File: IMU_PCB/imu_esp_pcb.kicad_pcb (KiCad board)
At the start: 2 copper layers, 19 parts, among them J3 Conn_01x02_Pin, U1 MPU-6050, U2 ESP32-C3-WROOM-02, U3 PTS647SM38SMTR2LFS, U4 XC6206P332MR-G, U5 1N5819HW-7-F

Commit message: Add files via upload
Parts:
- added R4: 0, Resistor_SMD:R_0805_2012Metric_Pad1.20x1.40mm_HandSolder, F.Cu at (104.5, 87.0)
- added R5: 0, Resistor_SMD:R_0805_2012Metric_Pad1.20x1.40mm_HandSolder, F.Cu at (95.0, 90.5)
- added R6: 0, Resistor_SMD:R_0805_2012Metric_Pad1.20x1.40mm_HandSolder, F.Cu at (94.0, 71.0)
- moved C4 2.00 mm to (92.5, 84.5)
- moved C1 2.00 mm to (95.0, 84.5)
- moved C9 0.96 mm to (98.5, 80.5)
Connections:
- U1 pad 24: SDA -> Net-(U1-SDA)
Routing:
- net GND: track 2.65 -> 36.1 mm
- net SDA: track 14.8 -> 5.22 mm, vias 2 -> 0
- net Net-(U1-SDA): track 0.00 -> 6.98 mm
- net Net-(U4-VIN): track 11.6 -> 9.58 mm
- net Net-(U1-CPOUT): track 10.8 -> 9.54 mm
- net Net-(U1-REGOUT): track 8.42 -> 7.60 mm
- net Net-(U1-VLOGIC): track 8.65 -> 9.17 mm
- net +3.3V: track 90.9 -> 91.3 mm, vias 2 -> 0
- removed copper zone on B.Cu, net GND
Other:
- board outline added: 48.5 x 26 mm

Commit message: we're cooked
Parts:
- removed J3: Conn_01x02_Pin, Connector_PinHeader_2.54mm:PinHeader_1x02_P2.54mm_Vertical_SMD_Pin1Left
- removed UART1: UART, Connector_PinHeader_2.54mm:PinHeader_1x04_P2.54mm_Vertical
- added J1: Conn_01x02_Pin, Connector_PinHeader_2.54mm:PinHeader_1x02_P2.54mm_Vertical, F.Cu at (88.5, 87.0)
- added J2: Conn_01x05_Pin, Connector_PinHeader_2.54mm:PinHeader_1x05_P2.54mm_Vertical, F.Cu at (66.5, 75.9)
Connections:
- U1 pad 12: GND -> unconnected-(U1-INT-Pad12)
- U2 pad 11: unconnected-(U2-IO20/RXD-Pad11) -> TXD
- U2 pad 12: unconnected-(U2-IO21/TXD-Pad12) -> RXD
- U2 pad 6: Net-(U2-IO7) -> unconnected-(U2-IO7-Pad6)
- U2 pad 7: Net-(U2-IO8) -> unconnected-(U2-IO8-Pad7)
- U2 pad 8: unconnected-(U2-IO9-Pad8) -> Net-(J2-Pin_4)
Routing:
- net RXD: track 0.00 -> 27.8 mm
- net TXD: track 0.00 -> 27.0 mm
- net +3.3V: track 91.3 -> 117.7 mm
- net Net-(J2-Pin_4): track 0.00 -> 16.0 mm
- net GND: track 36.1 -> 45.7 mm, vias 0 -> 2
- net Net-(U2-IO8): track 8.33 -> 0.00 mm
- net Net-(U2-IO7): track 7.90 -> 0.00 mm
- net RESET: track 40.2 -> 43.1 mm
- net Net-(J1-Pin_1): track 4.96 -> 4.24 mm

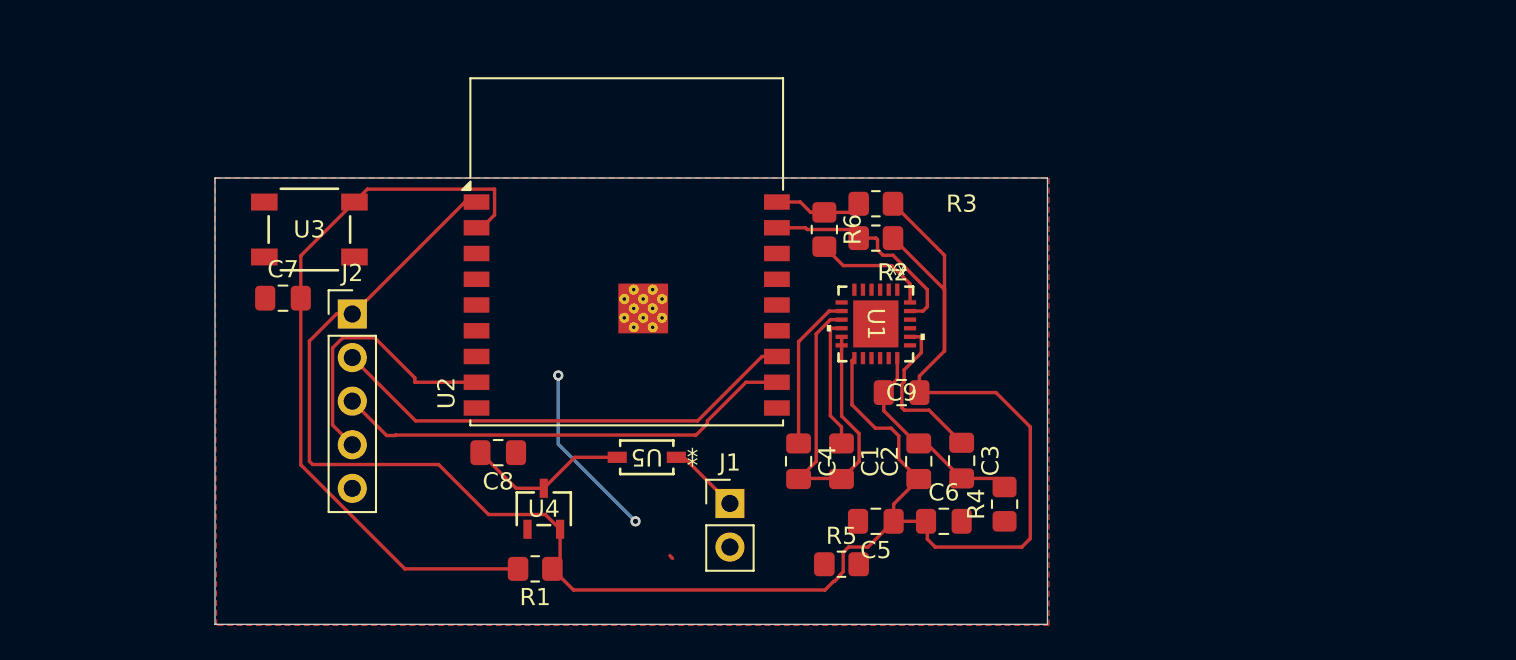
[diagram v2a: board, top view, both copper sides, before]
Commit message: Fixing PCB files from root
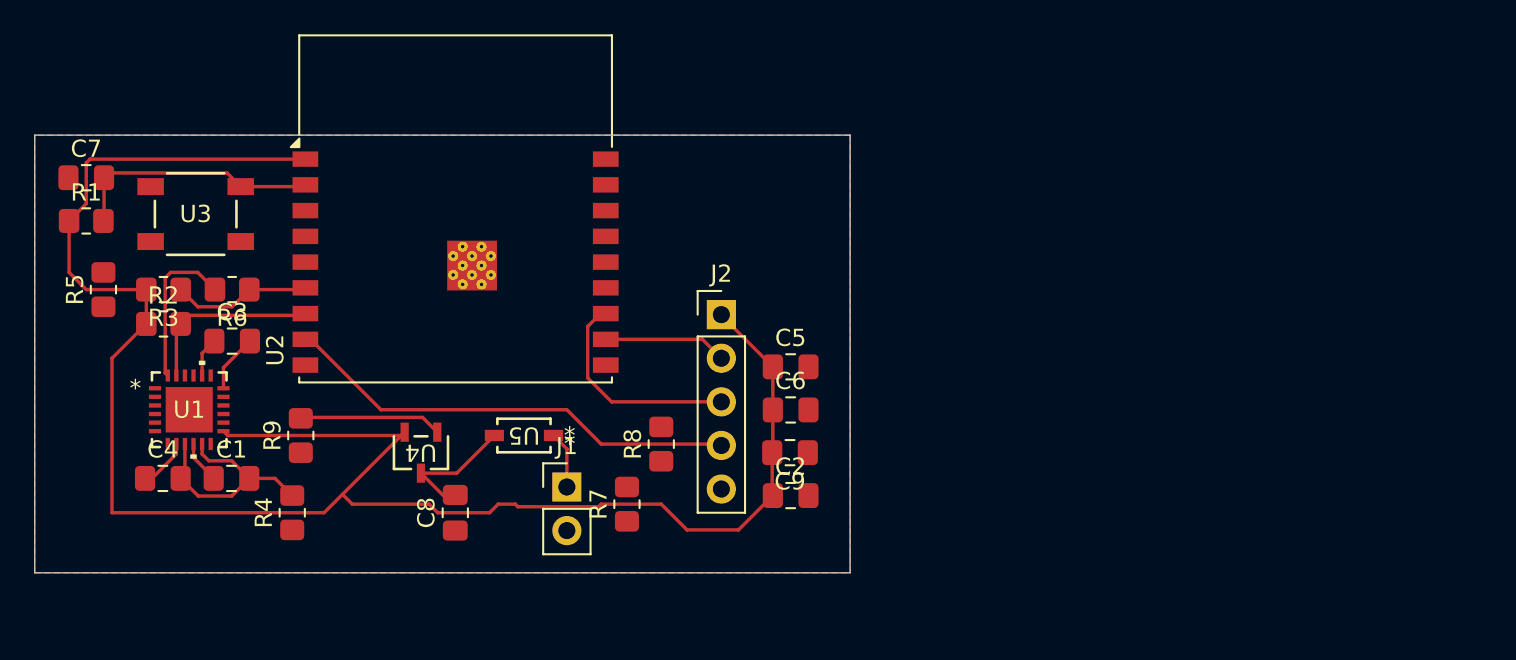
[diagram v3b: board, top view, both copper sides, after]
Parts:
- added R7: 0, Resistor_SMD:R_0805_2012Metric_Pad1.20x1.40mm_HandSolder, F.Cu at (82.5, 87.0)
- added R8: 0, Resistor_SMD:R_0805_2012Metric_Pad1.20x1.40mm_HandSolder, F.Cu at (84.5, 83.5)
- added R9: 0, Resistor_SMD:R_0805_2012Metric_Pad1.20x1.40mm_HandSolder, F.Cu at (63.5, 83.0)
- moved R5 45.9 mm to (52.0, 74.5), turned to 90 degrees
- moved C3 43.1 mm to (59.5, 77.5), turned to 0 degrees
- moved R2 41.8 mm to (55.5, 76.5), turned to 0 degrees
- moved R3 41.8 mm to (55.5, 74.5), turned to 180 degrees
- moved R4 41.5 mm to (63.0, 87.5)
- moved U1 40.3 mm to (57.0, 81.5), turned to 0 degrees
- moved C4 37.1 mm to (55.5, 85.5), turned to 0 degrees
- moved C1 35.6 mm to (59.5, 85.5), turned to 0 degrees
- moved R6 34.7 mm to (59.5, 74.5), turned to 180 degrees
- moved R1 33.1 mm to (51.0, 70.5), turned to 0 degrees
- moved J2 21.5 mm to (88.0, 76.0)
- moved C7 13.4 mm to (51.0, 68.0)
- moved C6 11.0 mm to (92.0, 81.5)
- moved U2 10.3 mm to (72.5, 72.9)
- moved C5 10.3 mm to (92.0, 79.0), turned to 0 degrees
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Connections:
- U2 pad 11: TXD -> RXD
- U2 pad 12: RXD -> TXD
- U2 pad 17: SCL -> unconnected-(U2-IO1-Pad17)
- U2 pad 18: SDA -> unconnected-(U2-IO0-Pad18)
- U2 pad 6: unconnected-(U2-IO7-Pad6) -> SDA
- U2 pad 7: unconnected-(U2-IO8-Pad7) -> SCL
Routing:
- net RESET: track 43.1 -> 14.8 mm
- net RXD: track 27.8 -> 7.19 mm
- net GND: track 45.7 -> 25.5 mm, vias 2 -> 0
- net TXD: track 27.0 -> 12.7 mm
- net Net-(J2-Pin_4): track 16.0 -> 26.8 mm
- net +3.3V: track 117.7 -> 107.2 mm
- net Net-(U1-CPOUT): track 9.54 -> 2.30 mm
- net Net-(U1-VLOGIC): track 9.17 -> 3.00 mm
- net Net-(U1-REGOUT): track 7.60 -> 2.51 mm
- net SDA: track 5.22 -> 8.14 mm
- net Net-(U1-SDA): track 6.98 -> 9.20 mm
- net SCL: track 12.7 -> 10.6 mm
- net Net-(U4-VIN): track 9.58 -> 7.71 mm
- net Net-(J1-Pin_1): track 4.24 -> 3.32 mm
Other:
- board size 48.5 x 26 mm -> 47.5 x 25.5 mm
